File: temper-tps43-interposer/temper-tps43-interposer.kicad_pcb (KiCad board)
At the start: 2 copper layers, 34 x 44 mm, 5 parts, among them CON1 TPS43 FFC

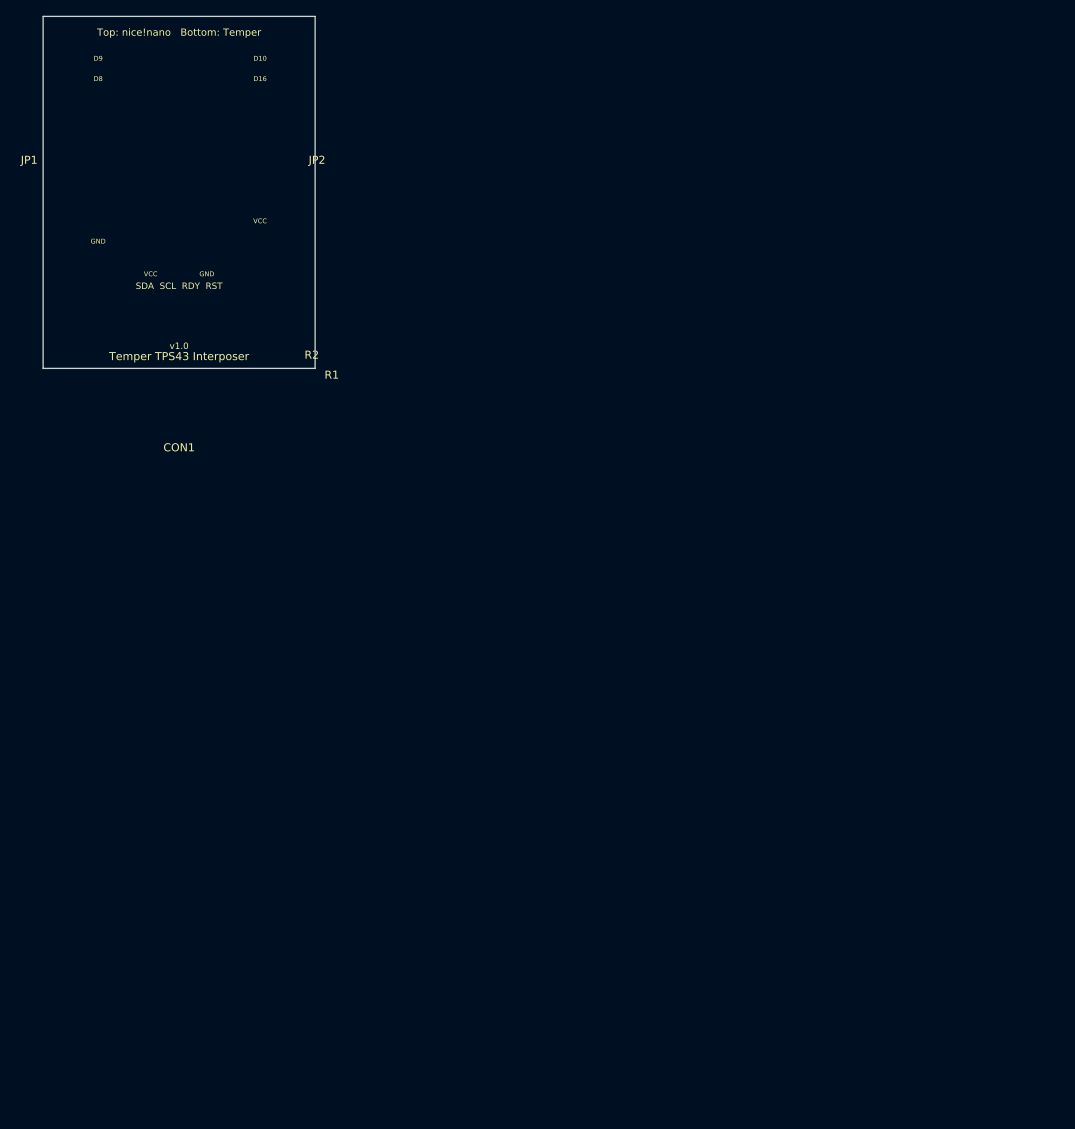
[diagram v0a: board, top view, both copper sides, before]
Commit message: Rebuild TPS43 interposer from scratch for KiCad 10
Replaces the hand-written KiCad 9 board with a generated one. gen_schematic.py
owns the netlist table and gen_interposer.py imports it, so the schematic and
the board cannot drift. build.sh gates on ERC, DRC and schematic parity, all of
which are clean.

Sized and verified against the actual Temper hardware (raeedcho/temper) rather
than the old spec:

- 20.0 x 40.0 mm, down from 34 x 44. Temper's choc hotswap sockets end 1.60 mm
  from the controller footprint, so the old width sat 6.44 mm over the adjacent
  switch column and overhung the right board edge by 6.76 mm.
- Notched south edge to clear Temper's nice!view header J2, which starts level
  with header pin 12.
- D8/D9/D10/D16 confirmed unconnected in Temper's netlist.

Corrected errors carried over from the old spec:

- FFC pinout was invented. The TPS43's J1 is 1:RDY 2:NRST 3:GND 4:VDDHI 5:SCL
  6:SDA (datasheet rev 1.06). The old order matched neither that nor its
  reversal, and would have driven 3.3 V onto RDY and shorted SCL to ground.
  CON1 is now derived from TPS43_J1 and checked by verify_pinout().
- D9 is P1.06, D10 is P0.09, D16 is P0.10. The overlay's TWIM_SCL psel was on
  P0.09, which is D10, so I2C could never have come up. P0.11, claimed for D10,
  is D7, one of Temper's matrix rows.
- CONFIG_NFCT_PINS_AS_GPIOS is required: RDY and NRST land on the NFC pins.
- Temper uses Mill-Max 310 machine sockets, which 2.54 mm square header pins do
  not fit. BOM is now Mill-Max pins and sockets.
- R1/R2 at 2.5 mm spacing collided; 0805 courtyard is 3.36 x 1.9 mm.
- Custom Molex footprint used non-plated mounting holes, giving the connector no
  retention. Replaced with the stock Hirose FH12-6S-0.5SH footprint.
- Headers on the wrong faces. Sockets go on top, pins on the bottom.

Open item: the FFC cable mapping cannot be resolved from any datasheet. The
board assumes a reversed cable (CON1 pin N to TPS43 pin 7-N) and the docs
describe the continuity chec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
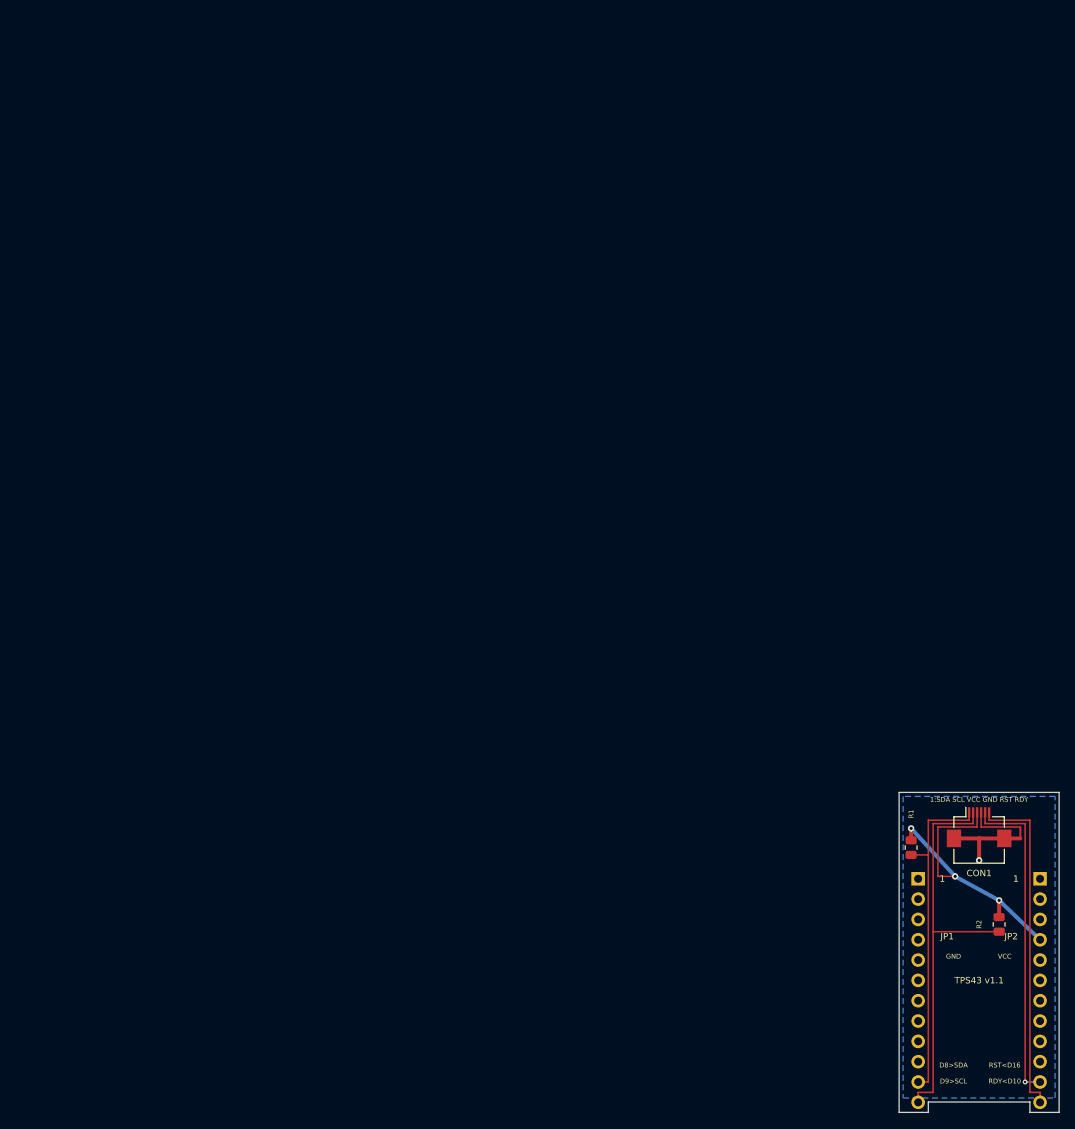
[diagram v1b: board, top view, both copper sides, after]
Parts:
- CON1: value TPS43 FFC -> FFC 1x06 0.5mm; footprint temper-tps43-interposer:TPS43_FFC_06 -> Connector_FFC-FPC:Hirose_FH12-6S-0.5SH_1x06-1MP_P0.50mm_Horizontal
- JP1: value ProMicro Left -> Pro Micro L
- JP2: value ProMicro Right -> Pro Micro R
- moved JP1 133.6 mm to (92.4, 87.3)
- moved JP2 133.6 mm to (107.6, 87.3)
- moved R2 129.8 mm to (102.5, 93.0), turned to -90 degrees
- moved CON1 119.4 mm to (100.0, 80.8)
- moved R1 113.9 mm to (91.5, 83.4), turned to -90 degrees
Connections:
- CON1 pad 1: VCC -> SDA
- CON1 pad 2: SDA -> SCL
- CON1 pad 3: SCL -> VCC
- CON1 pad 4: RDY -> GND
- CON1 pad 6: GND -> RDY
- JP1 pad 1: (no net) -> unconnected-(JP1-Pin_1-Pad1)
- JP1 pad 10: (no net) -> unconnected-(JP1-Pin_10-Pad10)
- JP1 pad 2: (no net) -> unconnected-(JP1-Pin_2-Pad2)
- JP1 pad 5: (no net) -> unconnected-(JP1-Pin_5-Pad5)
- JP1 pad 6: (no net) -> unconnected-(JP1-Pin_6-Pad6)
- JP1 pad 7: (no net) -> unconnected-(JP1-Pin_7-Pad7)
- JP1 pad 8: (no net) -> unconnected-(JP1-Pin_8-Pad8)
- JP1 pad 9: (no net) -> unconnected-(JP1-Pin_9-Pad9)
- JP2 pad 1: (no net) -> unconnected-(JP2-Pin_1-Pad1)
- JP2 pad 10: (no net) -> unconnected-(JP2-Pin_10-Pad10)
- JP2 pad 3: (no net) -> unconnected-(JP2-Pin_3-Pad3)
- JP2 pad 5: (no net) -> unconnected-(JP2-Pin_5-Pad5)
- JP2 pad 6: (no net) -> unconnected-(JP2-Pin_6-Pad6)
- JP2 pad 7: (no net) -> unconnected-(JP2-Pin_7-Pad7)
- JP2 pad 8: (no net) -> unconnected-(JP2-Pin_8-Pad8)
- JP2 pad 9: (no net) -> unconnected-(JP2-Pin_9-Pad9)
- R1 pad 1: SDA -> VCC
- R1 pad 2: VCC -> SDA
- R2 pad 1: SCL -> VCC
- R2 pad 2: VCC -> SCL
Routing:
- net SCL: track 0.00 -> 51.4 mm
- net RDY: track 0.00 -> 42.6 mm
- net SDA: track 0.00 -> 42.2 mm
- net RST: track 0.00 -> 40.6 mm, vias 0 -> 1
- net VCC: track 0.00 -> 40.1 mm, vias 0 -> 3
- net GND: track 0.00 -> 19.2 mm, vias 0 -> 1
- added copper zone on B.Cu, net GND
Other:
- board size 34 x 44 mm -> 20 x 40 mm
- board text added: "1"
- board text added: "1:SDA SCL VCC GND RST RDY"
- board text added: "20.0 x 40.0 x 1.0mm 2L FR4 1oz ENIG"
- board text added: "D8>SDA"
- board text added: "D9>SCL"
- board text added: "RDY<D10"
- board text added: "RST<D16"
- board text added: "TPS43 interp"
- board text added: "TPS43 v1.1"
- board text added: "v1.1 nano up"
- board text removed: "D10"
- board text removed: "D16"
- board text removed: "D8"
- board text removed: "D9"
- board text removed: "SDA SCL RDY RST"
- board text removed: "Temper TPS43 Interposer"
- board text removed: "Top: nice!nano Bottom: Temper"
- board text removed: "VCC GND"
- board text removed: "v1.0"
